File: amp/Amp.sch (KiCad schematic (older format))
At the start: 31 parts

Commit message: getting close on the amp
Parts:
- removed Q? (x2): 2N5457_NonStock, digikey-footprints:TO-92-3, symbol 2N5457_NonStock
- removed R1, R? (x10): 100K, symbol R
- removed R? (x2): 1K5, symbol R
- removed R? (x5): 1K, symbol R
- removed U? (x3): TL072, symbol TL072
- added C?: 30p, symbol C
- added Q? (x4): MAT02, TO-78, symbol MAT02
- added R? (x3): 1K, symbol R
- added R? (x2): 470, symbol R
- added R? (x3): 100K, symbol R
- added R?: 2K2, symbol R
- added R?: 4K7, symbol R
- added R?: 470K, symbol R
- added R? (x2): 10K, symbol R
- added RV?: POT, symbol POT
- added U? (x2): TL072, symbol TL072
- R?: value 100K -> 470K
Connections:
- net labels removed: M_CV
- wire segments 79 -> 76
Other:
- note removed: "MASTER-VCO"
- moved on the sheet: C?, R?, U?, U?A

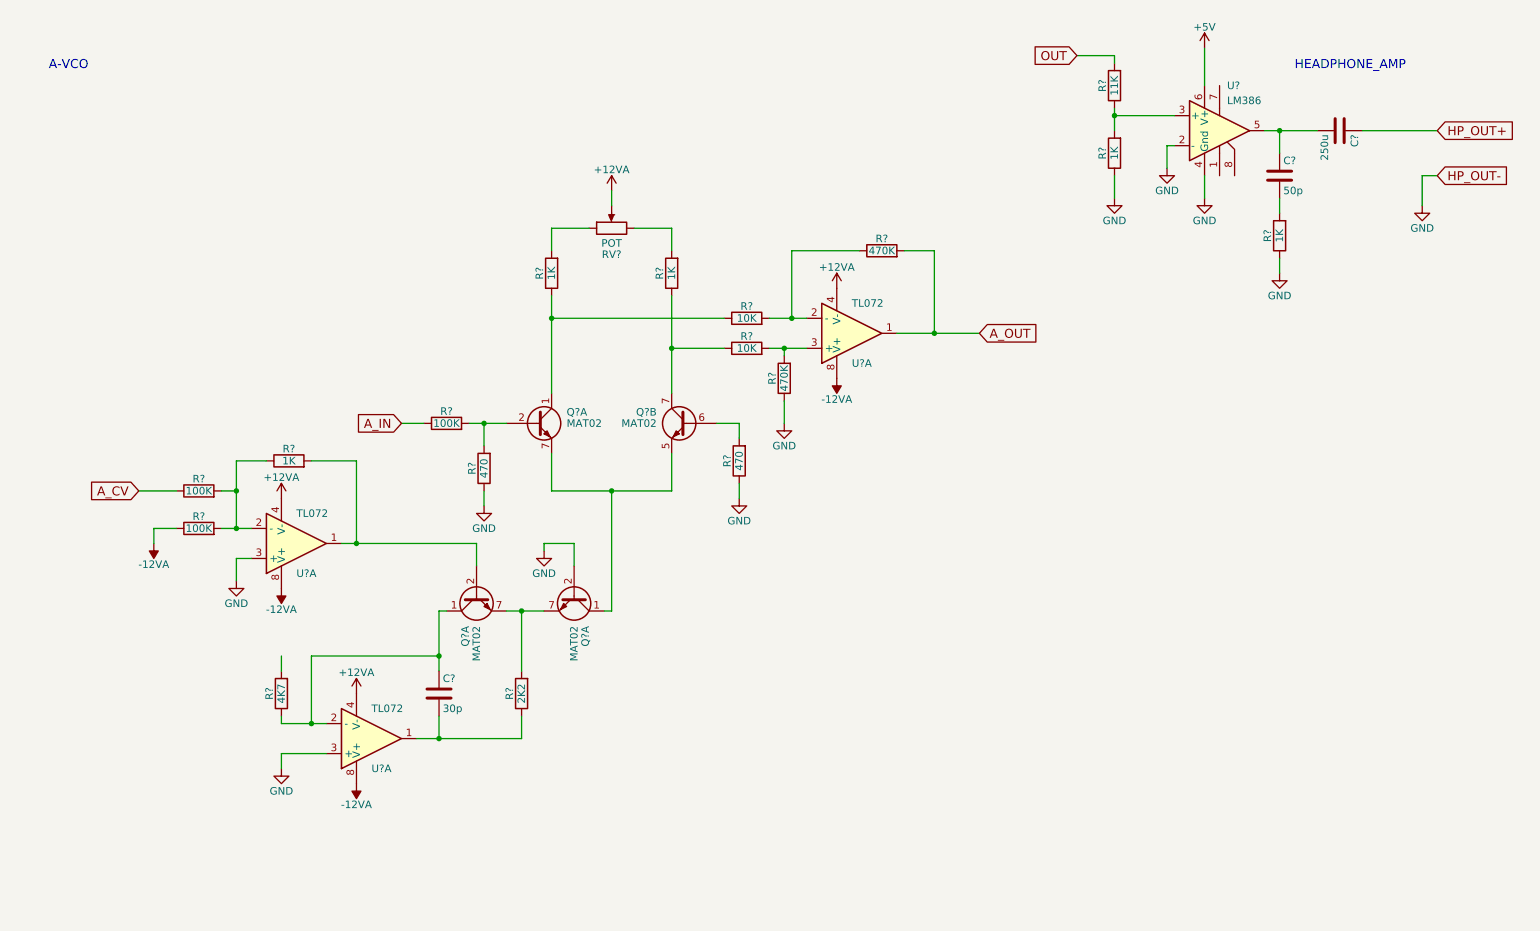
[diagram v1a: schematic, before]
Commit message: updated amp - LM13700 with PNP-exp. control
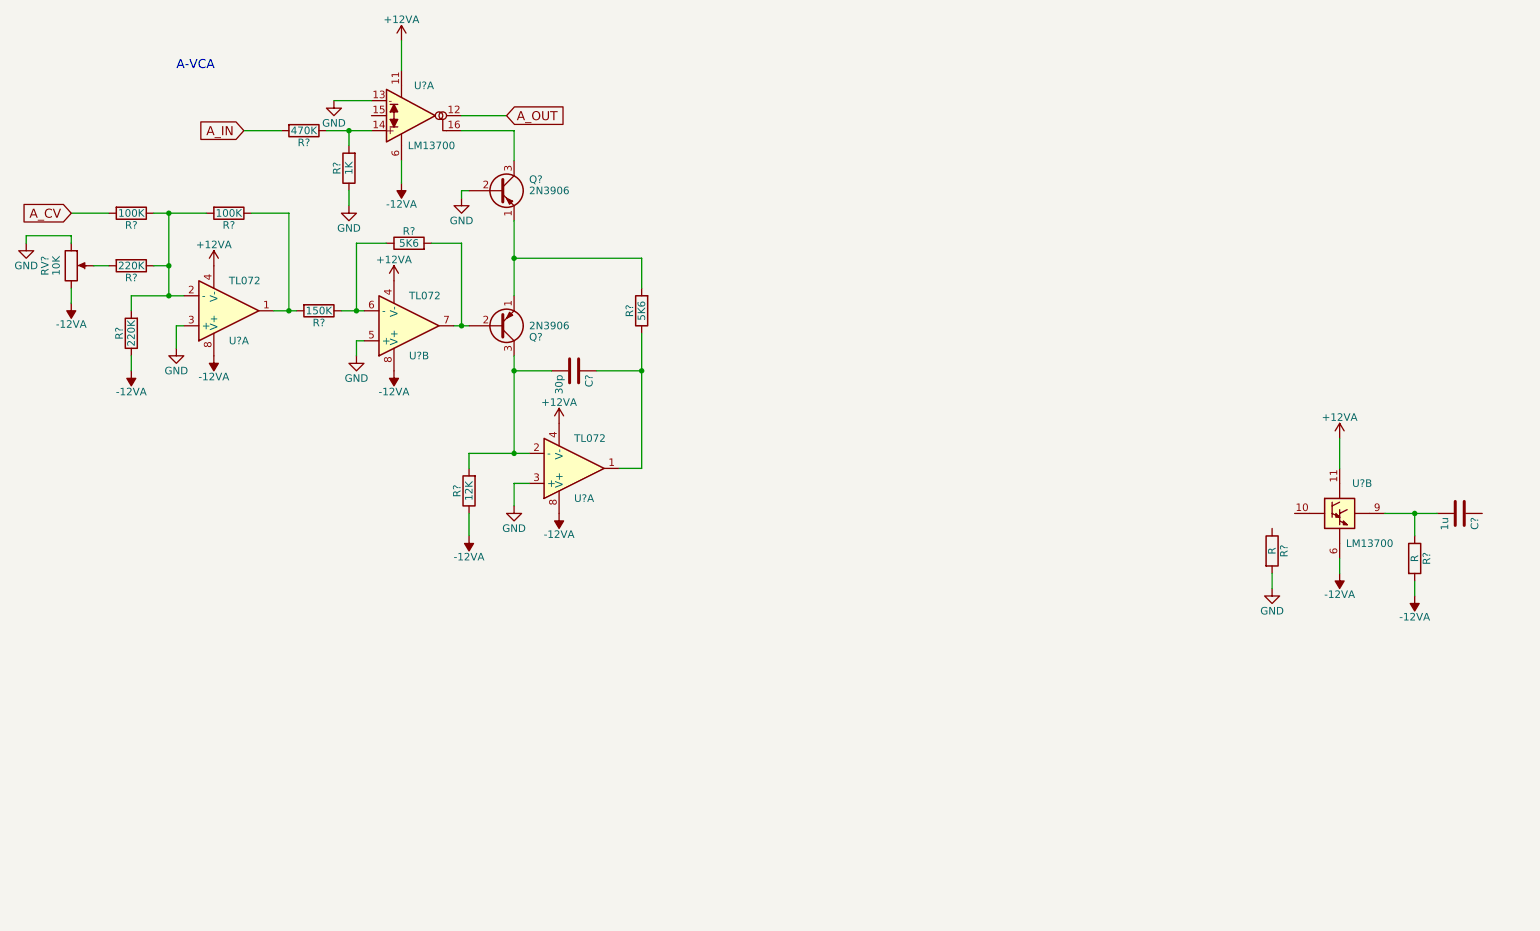
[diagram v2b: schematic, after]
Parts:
- removed C?: 50p, symbol C
- removed C?: 250u, symbol C
- removed Q? (x4): MAT02, TO-78, symbol MAT02
- removed R? (x2): 470K, symbol R
- removed R?: 11K, symbol R
- removed R? (x5): 1K, symbol R
- removed R? (x2): 470, symbol R
- removed R? (x3): 100K, symbol R
- removed R? (x2): 10K, symbol R
- removed RV?: POT, symbol POT
- removed U? (x2): TL072, symbol TL072
- removed U?: LM386, symbol LM386
- added C?: 1u, symbol C
- added Q? (x2): 2N3906, TO_SOT_Packages_THT:TO-92_Molded_Narrow, symbol 2N3906
- added R? (x2): R, symbol R
- added R?: 1K, symbol R
- added R?: 470K, symbol R
- added R?: 5K6, symbol R
- added R?: 150K, symbol R
- added R? (x2): 100K, symbol R
- added R? (x2): 220K, symbol R
- added RV?: 10K, symbol POT
- added U? (x2): LM13700, symbol LM13700
- added U? (x2): TL072, symbol TL072
- R?: value 2K2 -> 5K6
- R?: value 4K7 -> 12K
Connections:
- net +12VA: now also U?.11 (V+), U?.11 (V+), U?.4 (V-), U?.4 (V-)
- net -12VA: now also R?.1, R?.1, R?.2, RV?.3, U?.6 (V-), U?.6 (V-), U?.8 (V+), U?.8 (V+)
- net A_CV: now also R?.2
- net A_IN: now also R?.2
- net A_OUT: now also U?.12 (OUTPUT)
- net GND: now also Q?.2 (B), R?.1, R?.2, RV?.1, U?.13 (INPUT(-)), U?.3 (+), U?.5 (+)
- net at R?.2: now also Q?.1 (E), Q?.1 (E)
- net at R?.1, U?.1: now also C?.1; no longer C?.2
- net at R?.2: now also C?.2, U?.2 (-), Q?.3 (C)
- new net: R?.1, R?.2, U?.14 (INPUT(+))
- new net: Q?.3 (C), U?.16 (AMP_BIAS_INPUT)
- new net: C?.2, R?.1, U?.9 (BUFFER_OUTPUT)
- new net: Q?.2 (B), R?.2, U?.7
- new net: R?.1, R?.1, U?.6 (-)
- new net: R?.1, R?.2, U?.1
- new net: R?.2, RV?.2
- new net: R?.1, R?.1, R?.2, R?.2, U?.2 (-)
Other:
- note added: "A-VCA"
- note removed: "A-VCO"
- note removed: "HEADPHONE_AMP"
- moved on the sheet: C?, R?, U?A
